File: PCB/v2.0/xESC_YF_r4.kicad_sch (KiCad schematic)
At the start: 44 parts, among them J1 Conn_01x09_Male, J10 OM-MB W => MC BRK, J11 Conn_01x04_Pin, J2 Conn_01x02_Pin, J3 Conn_01x05_Male, J4 Conn_01x05_Male, J6 OM-MB U => MC SA, J7 Conn_01x06_Male, J8 Conn_01x06_Pin, J9 OM-MB V => MC +24V, Q1 BSS138, Q2 BSS138, Q3 BSS138, U1 STM32C011F6P6, U2 TPS1H200A, U3 INA139NA, U5 XC6220B331MR

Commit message: Add measurements
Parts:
- R5: value 220 -> 180; Digikey 311-220HRCT-ND -> (none); Part Number RC0603FR-07220RL -> RC0603FR-07180RL; Stock_PN R-603-220-.1W-1% -> R-603-180-.1W-1%
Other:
- note added: "TODO: ----- - Add Rs to UART2 - Add GND to UART2 connector - Move VMS_FAULT to free (non-NRST) GPIO - Add Pull-Up to INA - Change to Levelshifter IC? - Drop switchable INA gain - Increase R_Shunt for: Main range = 10mA -> 500mA Max = 1.5A"
- note added: "V_{Out}@Idle = 19mV V_{Out}@3500rpm = 530mV"
- note added: "V_{Shunt}@Idle = 0,7mV V_{Shunt}@3500rpm = 13mV"
- note removed: "TODO: ----- - Add Rs to UART2 - Add GND to UART2 connector - Move VMS_FAULT to free (non-NRST) GPIO - Add Pull-Up to INA - Change to Levelshifter IC? - Drop switchable INA gain? - Add "Messpoint" to VMS (for easier R_SHUNT measurement)"
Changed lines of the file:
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@@
 		)
 	)
-	(text "TODO:\n-----\n- Add Rs to UART2\n- Add GND to UART2 connector\n- Move VMS_FAULT to free (non-NRST) GPIO\n- Add Pull-Up to INA\n- Change to Levelshifter IC?\n- Drop switchable INA gain?\n- Add \"Messpoint\" to VMS\n  (for easier R_SHUNT measurement)"
+	(text "TODO:\n-----\n- Add Rs to UART2\n- Add GND to UART2 connector\n- Move VMS_FAULT to free (non-NRST) GPIO\n- Add Pull-Up to INA\n- Change to Levelshifter IC?\n- Drop switchable INA gain\n- Increase R_Shunt for:\n  Main range = 10mA -> 500mA\n  Max = 1.5A"
 		(exclude_from_sim no)
 		(at -38.1 21.59 0)
@@
 			(font
 				(size 1.27 1.27)
+			)
+			(justify left)
+		)
+	)
+	(text "V_{Out}@Idle = 19mV\nV_{Out}@3500rpm = 530mV"
+		(exclude_from_sim no)
+		(at 175.768 75.692 0)
+		(effects
+			(font
+				(size 1.27 1.27)
+				(color 194 0 194 1)
+			)
+			(justify left)
+		)
+	)
+	(text "V_{Shunt}@Idle = 0,7mV\nV_{Shunt}@3500rpm = 13mV"
+		(exclude_from_sim no)
+		(at 232.41 75.692 0)
+		(effects
+			(font
+				(size 1.27 1.27)
+				(color 194 0 194 1)
 			)
 			(justify left)
@@
 			)
 		)
-		(property "Value" "220"
+		(property "Value" "180"
 			(at 95.758 171.323 0)
 			(effects
@@
 			)
 		)
-		(property "Digikey" "311-220HRCT-ND"
+		(property "Part Number" "RC0603FR-07180RL"
 			(at 93.98 170.18 0)
 			(effects
@@
 			)
 		)
-		(property "Part Number" "RC0603FR-07220RL"
+		(property "Stock_PN" "R-603-180-.1W-1%"
 			(at 93.98 170.18 0)
 			(effects
-				(font
-					(size 1.27 1.27)
-				)
-				(hide yes)
-			)
-		)
-		(property "Stock_PN" "R-603-220-.1W-1%"
-			(at 93.98 170.18 0)
-			(effects

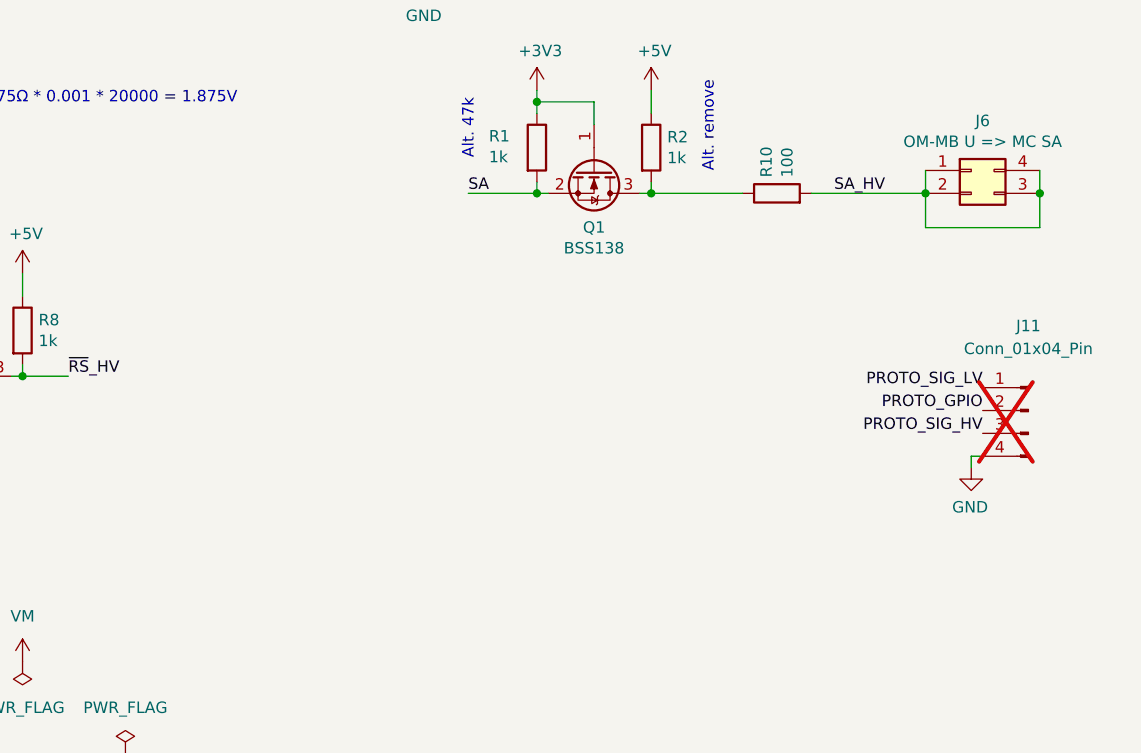
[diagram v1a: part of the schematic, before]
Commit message: Add shutdown signal handling
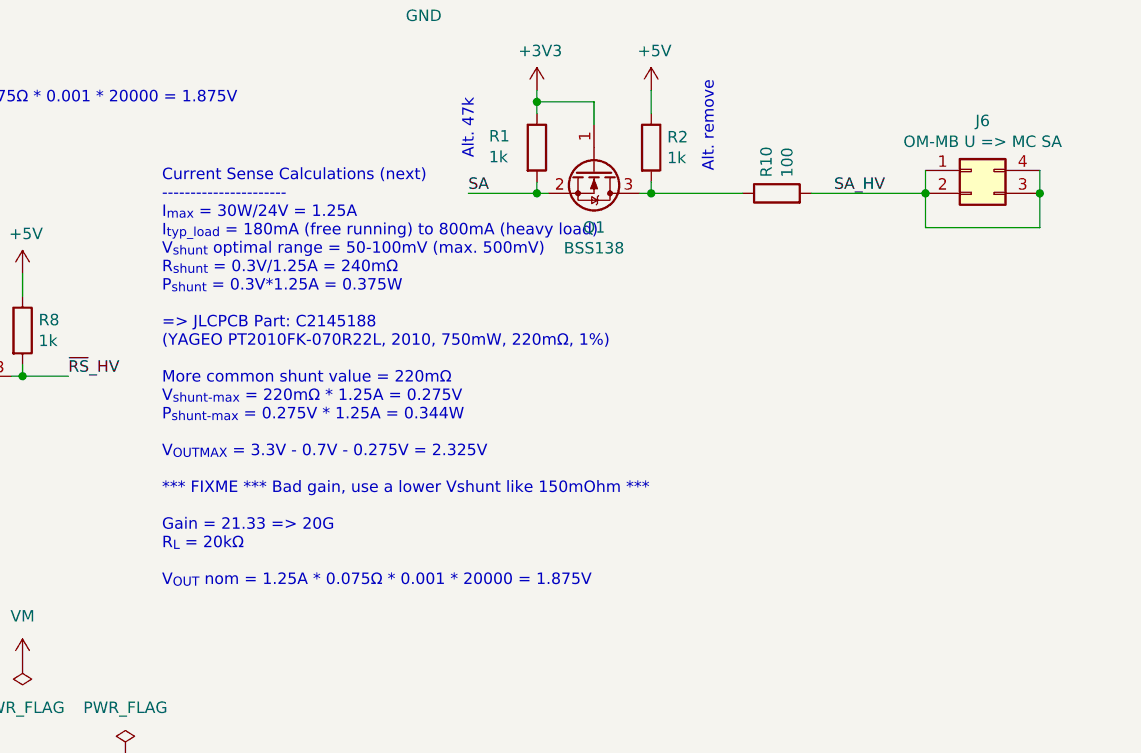
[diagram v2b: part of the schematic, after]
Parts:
- removed J11: Conn_01x04_Pin, Connector_PinHeader_2.54mm:PinHeader_1x04_P2.54mm_Vertical, symbol Connector:Conn_01x04_Pin
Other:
- note added: "Current Sense Calculations (next) ---------------------- I_{max} = 30W/24V = 1.25A I_{typ_load} = 180mA (free running) to 800mA (heavy load) V_{shunt} optimal range = 50-100mV (max. 500mV) R_{shunt} = 0.3V/1.25A = 240mΩ P_{shunt} = 0.3V*1.25A = 0.375W => JLCPCB Part: C2145188 (YAGEO PT2010FK-070R22L, 2010, 750mW, 220mΩ, 1%) More common shunt value = 220mΩ V_{shunt-max} = 220mΩ * 1.25A = 0.275V P_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"
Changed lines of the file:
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@@
 	(wire
 		(pts
-			(xy 260.35 154.94) (xy 261.62 154.94)
-		)
-		(stroke
-			(width 0)
-			(type default)
-		)
-	)
-	(wire
-		(pts
 			(xy 29.21 104.14) (xy 38.1 104.14)
 		)
@@
 	(wire
 		(pts
-			(xy 260.35 156.21) (xy 260.35 154.94)
-		)
-		(stroke
-			(width 0)
-			(type default)
-		)
-	)
-	(wire
-		(pts
 			(xy 212.09 49.53) (xy 212.09 48.26)
 		)
@@
 		)
 	)
+	(text "Current Sense Calculations (next)\n----------------------\nI_{max} = 30W/24V = 1.25A\nI_{typ_load} = 180mA (free running) to 800mA (heavy load)\nV_{shunt} optimal range = 50-100mV (max. 500mV)\nR_{shunt} = 0.3V/1.25A = 240mΩ\nP_{shunt} = 0.3V*1.25A = 0.375W\n\n=> JLCPCB Part: C2145188\n(YAGEO PT2010FK-070R22L, 2010, 750mW, 220mΩ, 1%)\n\nMore common shunt value = 220mΩ\nV_{shunt-max} = 220mΩ * 1.25A = 0.275V\nP_{shunt-max} = 0.275V * 1.25A = 0.344W\n\nV_{OUTMAX} = 3.3V - 0.7V - 0.275V = 2.325V\n\n*** FIXME *** Bad gain, use a lower Vshunt like 150mOhm ***\n\nGain = 21.33 => 20G\nR_{L} = 20kΩ\n\nV_{OUT} nom = 1.25A * 0.075Ω * 0.001 * 20000 = 1.875V\n"
+		(exclude_from_sim no)
+		(at 170.434 146.304 0)
+		(effects
+			(font
+				(size 1.27 1.27)
+			)
+			(justify left)
+		)
+	)
 	(text "Alt. remove"
 		(exclude_from_sim no)
@@
 		)
 	)
-	(label "PROTO_SIG_LV"
-		(at 261.62 147.32 180)
-		(fields_autoplaced yes)
-		(effects
-			(font
-				(size 1.27 1.27)
-			)
-			(justify right bottom)
-		)
-	)
 	(label "SWCLK"
 		(at 38.1 99.06 0)
@@
 		)
 	)
-	(label "PROTO_SIG_HV"
-		(at 261.62 152.4 180)
-		(fields_autoplaced yes)
-		(effects
-			(font
-				(size 1.27 1.27)
-			)
-			(justify right bottom)
-		)
-	)
 	(label "PROTO_GPIO"
 		(at 113.03 118.11 0)
@@
 		)
 	)
-	(label "PROTO_GPIO"
-		(at 261.62 149.86 180)
-		(fields_autoplaced yes)
-		(effects
-			(font
-				(size 1.27 1.27)
-			)
-			(justify right bottom)
-		)
-	)
 	(label "~{VMS_FAULT}{slash}NRST"
 		(at 38.1 106.68 0)
@@
 	)
 	(symbol
-		(lib_id "Connector:Conn_01x04_Pin")
-		(at 266.7 149.86 0)
-		(mirror y)
-		(unit 1)
-		(exclude_from_sim no)
-		(in_bom no)
-		(on_board yes)
-		(dnp yes)
-		(property "Reference" "J11"
-			(at 266.7 140.462 0)
-			(effects
-				(font
-					(size 1.27 1.27)
-				)
-			)
-		)
-		(property "Value" "Conn_01x04_Pin"
-			(at 266.7 143.002 0)
-			(effects
-				(font
-					(size 1.27 1.27)
-				)
-			)
-		)
-		(property "Footprint" "Connector_PinHeader_2.54mm:PinHeader_1x04_P2.54mm_Vertical"
-			(at 266.7 149.86 0)
-			(effects
-				(font
-					(size 1.27 1.27)
-				)
-				(hide yes)
-			)
-		)
-		(property "Datasheet" "~"
-			(at 266.7 149.86 0)
-			(effects
-				(font
-					(size 1.27 1.27)
-				)
-				(hide yes)
-			)
-		)
-		(property "Description" "Generic connector, single row, 01x04, script generated"
-			(at 266.7 149.86 0)
-			(effects
-				(font
-					(size 1.27 1.27)
-				)
-				(hide yes)
-			)
-		)
-		(pin "3"
-		)
-		(pin "4"
-		)
-		(pin "2"
-		)
-		(pin "1"
-		)
-		(instances
-			(project "xESC_YF_r4"
-				(path "/f1d82565-2f45-4436-9c4d-3203604bc842"
-					(reference "J11")
-					(unit 1)
-				)
-			)
-		)
-	)
-	(symbol
 		(lib_id "Connector:Conn_01x02_Pin")
 		(at 24.13 74.93 0)
@@
 					(unit 1)
 				)
-			)
-		)
-	)
-	(symbol
-		(lib_id "power:GND")
-		(at 260.35 156.21 0)
-		(mirror y)
-		(unit 1)
-		(exclude_from_sim no)
-		(in_bom yes)
-		(on_board yes)
-		(dnp no)
-		(property "Reference" "#PWR024"
-			(at 260.35 162.56 0)
-			(effects
-				(font
-					(size 1.27 1.27)
-				)
-				(hide yes)
-			)
-		)
-		(property "Value" "GND"
-			(at 260.223 160.6042 0)
-			(effects
-				(font
-					(size 1.27 1.27)
-				)
-			)
-		)
-		(property "Footprint" ""
-			(at 260.35 156.21 0)
-			(effects
-				(font
-					(size 1.27 1.27)
-				)
-				(hide yes)
-			)
-		)
-		(property "Datasheet" ""
-			(at 260.35 156.21 0)
-			(effects
-				(font
-					(size 1.27 1.27)
-				)
-				(hide yes)
-			)
-		)
-		(property "Description" "Power symbol creates a global label with name \"GND\" , ground"
-			(at 260.35 156.21 0)
-			(effects
-				(font
-					(size 1.27 1.27)
-				)
-				(hide yes)
-			)
-		)
-		(pin "1"
-		)
-		(instances
-			(project "xESC_YF_r4"
-				(path "/f1d82565-2f45-4436-9c4d-3203604bc842"
-					(reference "#PWR024")
-					(unit 1)
-				)

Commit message: Add HW v2.0
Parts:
- removed C24, C25: 4.7uF/16V, Capacitor_SMD:C_0603_1608Metric, symbol Device:C
- removed D3: S2MW, Diode_SMD:D_SOD-123F, symbol Device:D
- removed JP1: UART1_TX/UART2_TX, Jumper:SolderJumper-3_P1.3mm_Bridged12_RoundedPad1.0x1.5mm_NumberLabels, symbol Jumper:SolderJumper_3_Bridged12
- removed JP2: UART1_RX/UART2_RX, Jumper:SolderJumper-3_P1.3mm_Bridged12_RoundedPad1.0x1.5mm_NumberLabels, symbol Jumper:SolderJumper_3_Bridged12
- removed Q1, Q2, Q3: BSS138, Package_TO_SOT_SMD:SOT-23, symbol Transistor_FET:BSS138
- removed R13: 4k7, Resistor_SMD:R_0603_1608Metric, symbol Device:R
- removed R18: 220, Resistor_SMD:R_0603_1608Metric, symbol Device:R
- removed R3: 1k, Resistor_SMD:R_0805_2012Metric_Pad1.20x1.40mm_HandSolder, symbol Device:R
- removed U2: TPS1H200A, TPS1H200AQDGNRQ1.snapeda:SOP65P490X110-9N, symbol TPS1H200AQDGNRQ1:TPS1H200AQDGNRQ1
- removed U3: INA139NA, Package_TO_SOT_SMD:SOT-23-5, symbol Amplifier_Current:INA139
- removed U5: XC6220B331MR, Package_TO_SOT_SMD:SOT-23-5, symbol Regulator_Linear:XC6220B331MR
- added C1: 22uF, Capacitor_SMD:C_0805_2012Metric, symbol Device:C
- added C3: 22uF/10V, Capacitor_Tantalum_SMD:CP_EIA-3216-10_Kemet-I, symbol Device:C_Polarized
- added C4: .1uF, Capacitor_SMD:C_0402_1005Metric, symbol Device:C
- added D3: 1N5819WS, Diode_SMD:D_SOD-323, symbol Device:D_Schottky
- added D4: SM4007PL, Diode_SMD:D_SOD-123F, symbol Device:D
- added D5: 3V3, Diode_SMD:D_SOD-123F, symbol Device:D_Zener
- added HV_PB7, PA7, PB7: TestPoint_Flag, TestPoint:TestPoint_Pad_1.0x1.0mm, symbol Connector:TestPoint
- added JP1: SolderJumper_3_Bridged12, Jumper:SolderJumper-2_P1.3mm_Bridged_RoundedPad1.0x1.5mm, symbol Jumper:SolderJumper_2_Bridged
- added Q1, Q2, Q3, Q4: 2N7002, Package_TO_SOT_SMD:SOT-23, symbol Transistor_FET:2N7002
- added R14: 1k8, Resistor_SMD:R_0603_1608Metric, symbol Device:R
- added R16: 4k7, Resistor_SMD:R_0603_1608Metric, symbol Device:R
- added R17, R19, R20: 1k, Resistor_SMD:R_0603_1608Metric, symbol Device:R
- added U1: AMS1117-3.3, Package_TO_SOT_SMD:SOT-223-3_TabPin2, symbol Regulator_Linear:AMS1117-3.3
- added U3: TPS1H100BQPWPRQ1, Library:TPS1H100-Q1_ThermalVias, symbol xESC_YF_r4:TPS1H100B
- C2, C5: footprint Capacitor_SMD:C_0603_1608Metric -> Capacitor_SMD:C_0402_1005Metric; Digikey 1276-1935-1-ND -> (none); LCSC (none) -> C1525; Part Number CL10B104KC8NNNC -> (none); Stock_PN C-603-.1uF-100V-X7R -> C-402-.1uF-16V-X7R
- J2: value Conn_01x02_Pin -> Conn_01x03_Pin; footprint Connector_PinHeader_2.54mm:PinHeader_1x02_P2.54mm_Vertical -> Connector_PinHeader_2.54mm:PinHeader_1x03_P2.54mm_Vertical; symbol Connector:Conn_01x02_Pin -> Connector:Conn_01x03_Pin; now in the parts list
- J6: value OM-MB U => MC SA -> OM-MB U <= MC SA
- R1: value 1k -> 220; footprint Resistor_SMD:R_0805_2012Metric_Pad1.20x1.40mm_HandSolder -> Resistor_SMD:R_0603_1608Metric; LCSC (none) -> C22962; Stock_PN R-805-1K-.125W-1% -> (none)
- R10: value 100 -> 47k; LCSC (none) -> C25819; Part Number (none) -> 0603WAF4702T5E; Stock_PN (none) -> R-603-47K-.100W-1%
- R11: value 20k -> 47k; footprint Resistor_SMD:R_0402_1005Metric -> Resistor_SMD:R_0603_1608Metric; JLCPCB C2579762 -> (none); LCSC (none) -> C25819; Part Number RK73G1ETTP2002D -> 0603WAF4702T5E; Stock_PN R-0402-20000-0.1W-0.5% -> R-603-47K-.100W-1%
- R12: Digikey 311-150HRCT-ND -> (none); LCSC (none) -> C23162; Part Number RC0603FR-07150RL -> 0603WAF4701T5E; Stock_PN R-603-150-.1W-1% -> R-603-4700-.1W-1%
- R13: renamed from R14; Digikey 311-150HRCT-ND -> (none); LCSC (none) -> C23162; Part Number RC0603FR-07150RL -> 0603WAF4701T5E; Stock_PN R-603-150-.1W-1% -> R-603-4700-.1W-1%
- R15: value 20k -> 1k; footprint Resistor_SMD:R_0402_1005Metric -> Resistor_SMD:R_0603_1608Metric; JLCPCB C2579762 -> (none); LCSC (none) -> C21190; Part Number RK73G1ETTP2002D -> 0603WAF1001T5E; Stock_PN R-0402-20000-0.1W-0.5% -> R-603-1000-.1W-1%
- R18: renamed from R16; value 15k -> 10k; LCSC (none) -> C25804; Part Number (none) -> 0603WAF1002T5E; Stock_PN R-603-15000-.1W-1% -> R-603-10000-.1W-1%
- R2, R7: value 1k -> 220; footprint Resistor_SMD:R_0805_2012Metric_Pad1.20x1.40mm_HandSolder -> Resistor_SMD:R_0603_1608Metric; Digikey 311-1.00KCRCT-ND -> (none); LCSC C95781 -> C22962; Part Number RC0805FR-071KL -> (none); Stock_PN R-805-1K-.125W-1% -> (none)
- R3: renamed from R17; LCSC (none) -> C22962; Part Number (none) -> 0603WAF2200T5E
- R4: value 1k -> 220; footprint Resistor_SMD:R_0805_2012Metric_Pad1.20x1.40mm_HandSolder -> Resistor_SMD:R_0603_1608Metric; Digikey 311-1.00KCRCT-ND -> (none); LCSC C95781 -> C22962; Part Number RC0805FR-071KL -> 0603WAF2200T5E; Stock_PN R-805-1K-.125W-1% -> R-603-220-.1W-1%
- R5: value 180 -> 47k; LCSC (none) -> C25819; Part Number RC0603FR-07180RL -> 0603WAF4702T5E; Stock_PN R-603-180-.1W-1% -> R-603-47K-.100W-1%
- R6: value 220 -> 47k; Digikey 311-220HRCT-ND -> (none); LCSC (none) -> C25819; Part Number RC0603FR-07220RL -> 0603WAF4702T5E; Stock_PN R-603-220-.1W-1% -> R-603-47K-.100W-1%
- R8: value 1k -> 470; footprint Resistor_SMD:R_0805_2012Metric_Pad1.20x1.40mm_HandSolder -> Resistor_SMD:R_0603_1608Metric; Digikey 311-1.00KCRCT-ND -> (none); LCSC C95781 -> C23179; Part Number RC0805FR-071KL -> 0603WAF4700T5E; Stock_PN R-805-1K-.125W-1% -> R-603-470-.1W-1%
- R9: value 75mR -> 470; footprint Resistor_SMD:R_2010_5025Metric_Pad1.40x2.65mm_HandSolder -> Resistor_SMD:R_0603_1608Metric; JLCPCB C333474 -> (none); LCSC (none) -> C23179; Part Number RTT20R075FTE -> 0603WAF4700T5E; Stock_PN R-2010-.075-0.5W-1% -> R-603-470-.1W-1%
- renumbered U1 to U2
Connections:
- net +3V3: now also R11.1, R5.1, R8.2, C3.1, C4.1, Q1.1 (G), Q2.1 (G), Q3.1 (G), Q4.1 (G), R20.2, U1.2 (VO); no longer C2.2, R1.1, R7.1
- net +5V: now also C2.1, R10.1, R6.1, R9.2, C1.1, JP1.2 (B), U1.3 (VI); no longer R2.1, R4.1, R8.1
- net BRK: now also R8.1, U2.13 (PA6), Q2.2 (S); no longer U2.10 (PA3)
- net CUR_SENSE: now also U2.10 (PA3), D5.1 (K), R16.2; no longer R11.2, U2.9 (PA2)
- net GND: now also C2.2, J2.2 (Pin_2), C1.2, C3.2, C4.2, D4.1 (K), D5.2 (A), R17.2, U1.1 (GND); no longer C2.1
- net LED_GN: now also R1.1; no longer R5.1
- net LED_RD: now also R2.1, U2.20 (PB6); no longer R6.1, U2.2 (PC14)
- net SA: now also R5.2, U2.7 (PA0), Q1.2 (S); no longer R1.2, U2.1 (PB7)
- net SHUTDOWN: now also U2.2 (PC14); no longer U2.15 (PA8)
- net UART1_RX: now also J4.4 (Pin_4)
- net UART1_TX: now also R3.2
- net UART2_TX: now also R4.2; no longer J2.2 (Pin_2)
- net VM: now also U3.10 (VS), U3.8 (VS), U3.9 (VS)
- net VMS_DIAG_EN: now also U2.9 (PA2); no longer U2.20 (PB6)
- net VMS_IN: now also R12.1, U2.8 (PA1); no longer U2.7 (PA0)
- net at D1.2 (A): now also R1.2; no longer R5.2
- net at D2.2 (A): now also R2.2; no longer R6.2
- net at R13.2: now also U3.12 (DIAG_EN)
- net BRK_HV: no longer names the net of J10.1 (Pin_1), J10.2 (Pin_2), J10.3 (Pin_3), J10.4 (Pin_4)
- net BRK_HV: now also D3.1 (K); no longer R4.2
- removed net CUR_SENSE_2: R11.1, R15.2, U2.8 (PA1)
- net PROTO_GPIO: no longer names the net of U2.14 (PA7)
- net PROTO_GPIO: now also PA7.1
- net SA_HV renamed SA_TTL
- net SA_TTL: now also R7.2; no longer R10.2
- net VMC: no longer names the net of J9.1 (Pin_1), J9.2 (Pin_2), J9.3 (Pin_3), J9.4 (Pin_4)
- net VMC: now also R18.1, U3.5 (OUT), U3.6 (OUT), U3.7 (OUT); no longer R9.2
- net VMS: no longer names the net of R9.1
- net VMS: now also D3.2 (A), Q2.3 (D); no longer R18.1
- net ~{RS}_HV renamed ~{RS}_TTL
- net ~{RS}_TTL: now also R10.2, Q3.3 (D); no longer R8.2
- removed net ~{RS}_LV: R7.2, U2.13 (PA6)
- net ~{VMS_FAULT}/NRST renamed NRST
- net NRST: no longer R12.2
- new net: PB7.1, Q4.2 (S), R20.1, U2.1 (PB7)
- new net: JP1.1 (A), R19.2
- new net: HV_PB7.1, Q4.3 (D), R19.1
- new net: R16.1, R17.1, U3.14 (CS)
- new net: R14.2, U3.13 (CL)
- new net: D4.2 (A), R14.1, R15.2, U3.15 (GND), U3.2 (GND)
- new net: R12.2, U3.3 (IN)
- new net: J2.3 (Pin_3), R4.1
- new net: Q1.3 (D), R6.2, R7.1
- new net ~{RS}: Q3.2 (S), R11.2, U2.15 (PA8)
- no-connect marks 7 -> 6
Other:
- note added: "!!! GN/BK need to be exchanged on Mow-Motor-Plug or Cable !!!"
- note added: "!!! GN/BK need to be exchanged on Mow-Motor-Plug or Cable !!! Detectable via current correlation: With a wrong plug (GN/BK not exchanged), pulling SA output to 0 decrease current from 19mA to 12mA, which might be detectable. Whereas a correct plug (GN/BK got exchanged), pulling SA output to 0 increase current only from 11.3mA to 11.6mA. BUT NOT USABLE, BECAUSE ONCE GN (SA) GET CONNECTED WRONGLY T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"
- note added: "Current-Sense and Current-Limit Calculations ---------------------- Rev4 Motor specs: I_{nom} = 30W/24V = 1.25A I_{typ_load} = 180mA (free running) to 800mA (heavy load) I_{max} = 1.5A I_{idle} = 12mA Current-Sense calc: K = 500 R_{CS} = (V_{CS} * K) / I_{OUT} = (3V * 500) / 1.5A = 1000 Ohm I_{OUT} = 1.5A => V_{CS} = 3V V_{cs,H} >= 3.13V (usable ADC range = 0-3.1V) Current-Limit calc: V_{cl,th} =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"
- note added: "Open-Load = 2.4-2.9mA"
- note added: "R_{CL}"
- note added: "R_{CS}"
- note added: "TODO: -----"
- note removed: "!!! GN/BK need to be exchanged on Mow-Motor-Plug or Cable !!! Detectable via current correlation: With a wrong plug (GN/BK not exchanged), pulling SA output to 0 decrease current from 19mA to 12mA, which might be detectable. Whereas a correct plug (GN/BK got exchanged), pulling SA output to 0 increase current only from 11.3mA to 11.6mA."
- note removed: "Alt. 47k"
- note removed: "Alt. remove"
- note removed: "Current Sense Calculations (next) ---------------------- I_{max} = 30W/24V = 1.25A I_{typ_load} = 180mA (free running) to 800mA (heavy load) V_{shunt} optimal range = 50-100mV (max. 500mV) R_{shunt} = 0.3V/1.25A = 240mΩ P_{shunt} = 0.3V*1.25A = 0.375W => JLCPCB Part: C2145188 (YAGEO PT2010FK-070R22L, 2010, 750mW, 220mΩ, 1%) More common shunt value = 220mΩ V_{shunt-max} = 220mΩ * 1.25A = 0.275V P_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"
- note removed: "Current Sense Calculations ---------------------- I_{nom} = 30W/24V = 1.25A V_{shunt} full-scale target = 100mV (max. 500mV) R_{shunt} = 0.1V/1.25A = 80mΩ P_{shunt} = 0.1V*1.25A = 0.125W = 1/8W More common shunt value = 75mΩ V_{shunt} = 75mΩ * 1.25A = 0.09375V P_{shunt} = 0.09375V * 1.25A = 0.117W => 1/4W V_{OUTMAX} = 3.3V - 0.7V - 0.09375V = 2.506V V_{OUT} target = 2V Gain = 21.33 => 20G R_{L} =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"
- note removed: "TODO: ----- - Add Rs to UART2 - Add GND to UART2 connector - Move VMS_FAULT to free (non-NRST) GPIO - Add Pull-Up to INA - Change to Levelshifter IC? - Drop switchable INA gain - Increase R_Shunt for: Main range = 10mA -> 500mA Max = 1.5A"
- note removed: "V_{Out}@Idle = 19mV V_{Out}@3500rpm = 530mV"
- note removed: "V_{Shunt}@Idle = 0,7mV V_{Shunt}@3500rpm = 13mV"
- note removed: "int. PullUp = Auto-Retry?"
- moved on the sheet: J1, J10, J3, J4, J6, J7, J8, J9, R13, R18, R3, U2
